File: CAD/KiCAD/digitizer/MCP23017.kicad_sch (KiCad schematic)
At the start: 3 parts, among them P1b Conn_01x06, P3b Conn_01x10, P4a Conn_01x10

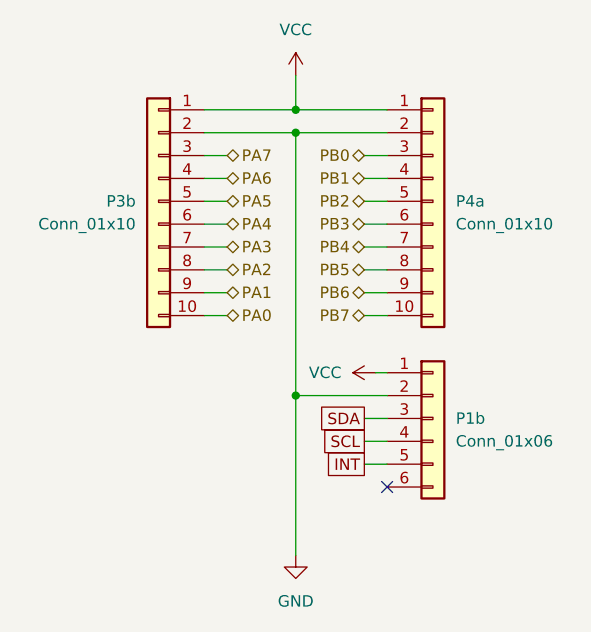
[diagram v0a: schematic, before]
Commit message: one MCP23017 added and routed
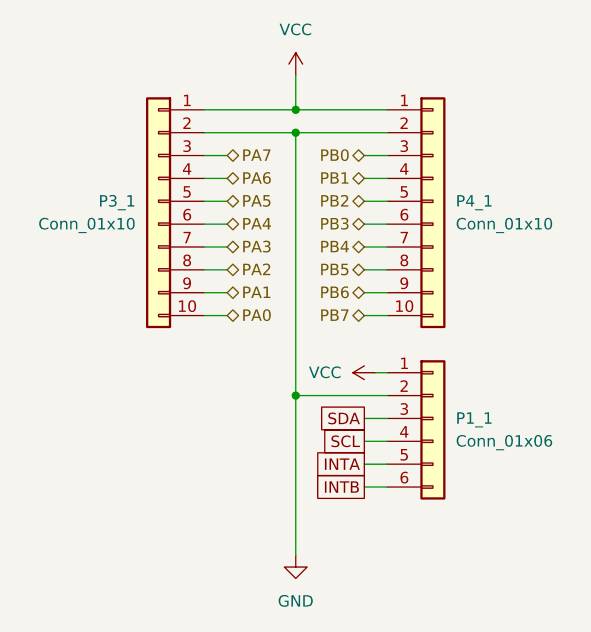
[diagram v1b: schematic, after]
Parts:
- P1_1: renamed from P1b; footprint Connector_PinHeader_2.54mm:PinHeader_1x06_P2.54mm_Vertical -> Connector_PinSocket_2.54mm:PinSocket_1x06_P2.54mm_Vertical
- P3_1: renamed from P3b; footprint Connector_PinHeader_2.54mm:PinHeader_1x10_P2.54mm_Vertical -> Connector_PinSocket_2.54mm:PinSocket_1x10_P2.54mm_Vertical
- P4_1: renamed from P4a; footprint Connector_PinHeader_2.54mm:PinHeader_1x10_P2.54mm_Vertical -> Connector_PinSocket_2.54mm:PinSocket_1x10_P2.54mm_Vertical
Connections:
- net INTB: now reaches P1_1.6 (Pin_6)
- net INT renamed INTA
- no-connect marks 1 -> 0
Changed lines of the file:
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@@
 		(color 0 0 0 0)
 	)
-	(no_connect
-		(at 111.76 102.87)
-	)
 	(wire
 		(pts
@@
 	(wire
 		(pts
+			(xy 109.22 102.87) (xy 111.76 102.87)
+		)
+		(stroke
+			(width 0)
+			(type default)
+		)
+	)
+	(wire
+		(pts
 			(xy 101.6 60.96) (xy 111.76 60.96)
 		)
@@
 		)
 	)
-	(global_label "INT"
+	(global_label "INTA"
 		(shape passive)
 		(at 109.22 100.33 180)
@@
 		)
 		(property "Intersheetrefs" "${INTERSHEET_REFS}"
-			(at 104.4432 100.33 0)
+			(at 103.3546 100.33 0)
 			(effects
 				(font
@@
 		(property "Intersheetrefs" "${INTERSHEET_REFS}"
 			(at 103.778 95.25 0)
+			(effects
+				(font
+					(size 1.27 1.27)
+				)
+				(justify right)
+				(hide yes)
+			)
+		)
+	)
+	(global_label "INTB"
+		(shape passive)
+		(at 109.22 102.87 180)
+		(fields_autoplaced yes)
+		(effects
+			(font
+				(size 1.27 1.27)
+			)
+			(justify right)
+		)
+		(property "Intersheetrefs" "${INTERSHEET_REFS}"
+			(at 103.1732 102.87 0)
 			(effects
 				(font
@@
 					(unit 1)
 				)
-				(path "/7204cdda-0a14-40c0-9dc8-8318dd514140/bcba0207-2ba5-46a1-aca2-aa24991baaf0"
-					(reference "#PWR06")
-					(unit 1)
-				)
 			)
 		)
@@
 		(dnp no)
 		(fields_autoplaced yes)
-		(property "Reference" "#PWR"
+		(property "Reference" "#PWR0101"
 			(at 101.6 60.96 0)
 			(effects
@@
 		(instances
 			(project "digitizer"
-				(path "/7204cdda-0a14-40c0-9dc8-8318dd514140/bcba0207-2ba5-46a1-aca2-aa24991baaf0"
-					(reference "#PWR03")
+				(path "/7204cdda-0a14-40c0-9dc8-8318dd514140/84745f20-6522-4018-95b9-58be475e1f2d"
+					(reference "#PWR0101")
 					(unit 1)
 				)
@@
 		(on_board yes)
 		(dnp no)
-		(property "Reference" "P3b"
+		(property "Reference" "P3_1"
 			(at 83.82 71.1199 0)
 			(effects
@@
 			)
 		)
-		(property "Footprint" "Connector_PinHeader_2.54mm:PinHeader_1x10_P2.54mm_Vertical"
+		(property "Footprint" "Connector_PinSocket_2.54mm:PinSocket_1x10_P2.54mm_Vertical"
 			(at 86.36 71.12 0)
 			(effects
@@
 		(instances
 			(project "digitizer"
-				(path "/7204cdda-0a14-40c0-9dc8-8318dd514140/bcba0207-2ba5-46a1-aca2-aa24991baaf0"
-					(reference "P3b")
+				(path "/7204cdda-0a14-40c0-9dc8-8318dd514140/84745f20-6522-4018-95b9-58be475e1f2d"
+					(reference "P3_1")
 					(unit 1)
 				)
@@
 		(dnp no)
 		(fields_autoplaced yes)
-		(property "Reference" "P4a"
+		(property "Reference" "P4_1"
 			(at 119.38 71.1199 0)
 			(effects
@@
 			)
 		)
-		(property "Footprint" "Connector_PinHeader_2.54mm:PinHeader_1x10_P2.54mm_Vertical"
+		(property "Footprint" "Connector_PinSocket_2.54mm:PinSocket_1x10_P2.54mm_Vertical"
 			(at 116.84 71.12 0)
 			(effects
@@
 			(project "digitizer"
 				(path "/7204cdda-0a14-40c0-9dc8-8318dd514140/84745f20-6522-4018-95b9-58be475e1f2d"
-					(reference "P4a")
-					(unit 1)
-				)
-				(path "/7204cdda-0a14-40c0-9dc8-8318dd514140/bcba0207-2ba5-46a1-aca2-aa24991baaf0"
-					(reference "P4b")
+					(reference "P4_1")
 					(unit 1)
 				)
@@
 					(unit 1)
 				)
-				(path "/7204cdda-0a14-40c0-9dc8-8318dd514140/bcba0207-2ba5-46a1-aca2-aa24991baaf0"
-					(reference "#PWR05")
-					(unit 1)
-				)
 			)
 		)
@@
 		(dnp no)
 		(fields_autoplaced yes)
-		(property "Reference" "P1b"
+		(property "Reference" "P1_1"
 			(at 119.38 95.2499 0)
 			(effects
@@
 			)
 		)
-		(property "Footprint" "Connector_PinHeader_2.54mm:PinHeader_1x06_P2.54mm_Vertical"
+		(property "Footprint" "Connector_PinSocket_2.54mm:PinSocket_1x06_P2.54mm_Vertical"
 			(at 116.84 95.25 0)
 			(effects
@@
 		(instances
 			(project "digitizer"
-				(path "/7204cdda-0a14-40c0-9dc8-8318dd514140/bcba0207-2ba5-46a1-aca2-aa24991baaf0"
-					(reference "P1b")
+				(path "/7204cdda-0a14-40c0-9dc8-8318dd514140/84745f20-6522-4018-95b9-58be475e1f2d"
+					(reference "P1_1")
 					(unit 1)
 				)

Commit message: routing wip take 1
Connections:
- net GND: no longer P3_1.2 (Pin_2), P4_1.2 (Pin_2)
- net VCC: no longer P3_1.1 (Pin_1), P4_1.1 (Pin_1)
- no-connect marks 0 -> 4
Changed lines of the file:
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@@
 	(generator_version "9.0")
 	(paper "USLetter")
-	(junction
-		(at 101.6 60.96)
-		(diameter 0)
-		(color 0 0 0 0)
-	)
-	(junction
-		(at 101.6 63.5)
-		(diameter 0)
-		(color 0 0 0 0)
-	)
-	(junction
-		(at 101.6 92.71)
-		(diameter 0)
-		(color 0 0 0 0)
+	(no_connect
+		(at 91.44 63.5)
+	)
+	(no_connect
+		(at 111.76 63.5)
+	)
+	(no_connect
+		(at 111.76 60.96)
+	)
+	(no_connect
+		(at 91.44 60.96)
 	)
 	(wire
@@
 	(wire
 		(pts
-			(xy 101.6 63.5) (xy 111.76 63.5)
-		)
-		(stroke
-			(width 0)
-			(type default)
-		)
-	)
-	(wire
-		(pts
 			(xy 91.44 76.2) (xy 93.98 76.2)
 		)
@@
 	(wire
 		(pts
-			(xy 101.6 57.15) (xy 101.6 60.96)
-		)
-		(stroke
-			(width 0)
-			(type default)
-		)
-	)
-	(wire
-		(pts
 			(xy 109.22 73.66) (xy 111.76 73.66)
 		)
@@
 	(wire
 		(pts
-			(xy 101.6 60.96) (xy 111.76 60.96)
-		)
-		(stroke
-			(width 0)
-			(type default)
-		)
-	)
-	(wire
-		(pts
-			(xy 91.44 60.96) (xy 101.6 60.96)
-		)
-		(stroke
-			(width 0)
-			(type default)
-		)
-	)
-	(wire
-		(pts
 			(xy 109.22 76.2) (xy 111.76 76.2)
 		)
@@
 		(pts
 			(xy 91.44 81.28) (xy 93.98 81.28)
-		)
-		(stroke
-			(width 0)
-			(type default)
-		)
-	)
-	(wire
-		(pts
-			(xy 101.6 63.5) (xy 101.6 92.71)
-		)
-		(stroke
-			(width 0)
-			(type default)
-		)
-	)
-	(wire
-		(pts
-			(xy 91.44 63.5) (xy 101.6 63.5)
 		)
 		(stroke
@@
 					(unit 1)
 				)
-			)
-		)
-	)
-	(symbol
-		(lib_id "power:VCC")
-		(at 101.6 57.15 0)
-		(unit 1)
-		(exclude_from_sim no)
-		(in_bom yes)
-		(on_board yes)
-		(dnp no)
-		(fields_autoplaced yes)
-		(property "Reference" "#PWR0101"
-			(at 101.6 60.96 0)
-			(effects
-				(font
-					(size 1.27 1.27)
-				)
-				(hide yes)
-			)
-		)
-		(property "Value" "VCC"
-			(at 101.6 52.07 0)
-			(effects
-				(font
-					(size 1.27 1.27)
-				)
-			)
-		)
-		(property "Footprint" ""
-			(at 101.6 57.15 0)
-			(effects
-				(font
-					(size 1.27 1.27)
-				)
-				(hide yes)
-			)
-		)
-		(property "Datasheet" ""
-			(at 101.6 57.15 0)
-			(effects
-				(font
-					(size 1.27 1.27)
-				)
-				(hide yes)
-			)
-		)
-		(property "Description" "Power symbol creates a global label with name \"VCC\""
-			(at 101.6 57.15 0)
-			(effects
-				(font
-					(size 1.27 1.27)
-				)
-				(hide yes)
-			)
-		)
-		(pin "1"
-		)
-		(instances
-			(project "digitizer"
-				(path "/7204cdda-0a14-40c0-9dc8-8318dd514140/84745f20-6522-4018-95b9-58be475e1f2d"
-					(reference "#PWR0101")
-					(unit 1)
-				)

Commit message: remove gerber files
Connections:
- net GND: now also P3_1.2 (Pin_2), P4_1.2 (Pin_2)
- net VCC: now also P3_1.1 (Pin_1), P4_1.1 (Pin_1)
- no-connect marks 4 -> 0
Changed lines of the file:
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@@
 	(generator_version "9.0")
 	(paper "USLetter")
-	(no_connect
-		(at 91.44 63.5)
-	)
-	(no_connect
-		(at 111.76 63.5)
-	)
-	(no_connect
-		(at 111.76 60.96)
-	)
-	(no_connect
-		(at 91.44 60.96)
+	(junction
+		(at 96.52 60.96)
+		(diameter 0)
+		(color 0 0 0 0)
+	)
+	(junction
+		(at 101.6 92.71)
+		(diameter 0)
+		(color 0 0 0 0)
+	)
+	(junction
+		(at 101.6 63.5)
+		(diameter 0)
+		(color 0 0 0 0)
 	)
 	(wire
@@
 	(wire
 		(pts
+			(xy 101.6 63.5) (xy 111.76 63.5)
+		)
+		(stroke
+			(width 0)
+			(type default)
+		)
+	)
+	(wire
+		(pts
+			(xy 96.52 60.96) (xy 111.76 60.96)
+		)
+		(stroke
+			(width 0)
+			(type default)
+		)
+	)
+	(wire
+		(pts
 			(xy 91.44 76.2) (xy 93.98 76.2)
 		)
@@
 	(wire
 		(pts
+			(xy 101.6 63.5) (xy 101.6 92.71)
+		)
+		(stroke
+			(width 0)
+			(type default)
+		)
+	)
+	(wire
+		(pts
 			(xy 91.44 68.58) (xy 93.98 68.58)
 		)
@@
 	(wire
 		(pts
+			(xy 96.52 57.15) (xy 96.52 60.96)
+		)
+		(stroke
+			(width 0)
+			(type default)
+		)
+	)
+	(wire
+		(pts
 			(xy 91.44 81.28) (xy 93.98 81.28)
 		)
@@
 	(wire
 		(pts
+			(xy 91.44 63.5) (xy 101.6 63.5)
+		)
+		(stroke
+			(width 0)
+			(type default)
+		)
+	)
+	(wire
+		(pts
 			(xy 109.22 71.12) (xy 111.76 71.12)
 		)
@@
 		(pts
 			(xy 101.6 92.71) (xy 111.76 92.71)
+		)
+		(stroke
+			(width 0)
+			(type default)
+		)
+	)
+	(wire
+		(pts
+			(xy 96.52 60.96) (xy 91.44 60.96)
 		)
 		(stroke
@@
 					(unit 1)
 				)
+			)
+		)
+	)
+	(symbol
+		(lib_id "power:VCC")
+		(at 96.52 57.15 0)
+		(unit 1)
+		(exclude_from_sim no)
+		(in_bom yes)
+		(on_board yes)
+		(dnp no)
+		(fields_autoplaced yes)
+		(property "Reference" "#PWR010"
+			(at 96.52 60.96 0)
+			(effects
+				(font
+					(size 1.27 1.27)
+				)
+				(hide yes)
+			)
+		)
+		(property "Value" "VCC"
+			(at 96.52 52.07 0)
+			(effects
+				(font
+					(size 1.27 1.27)
+				)
+			)
+		)
+		(property "Footprint" ""
+			(at 96.52 57.15 0)
+			(effects
+				(font
+					(size 1.27 1.27)
+				)
+				(hide yes)
+			)
+		)
+		(property "Datasheet" ""
+			(at 96.52 57.15 0)
+			(effects
+				(font
+					(size 1.27 1.27)
+				)
+				(hide yes)
+			)
+		)
+		(property "Description" "Power symbol creates a global label with name \"VCC\""
+			(at 96.52 57.15 0)
+			(effects
+				(font
+					(size 1.27 1.27)
+				)
+				(hide yes)
+			)
+		)
+		(pin "1"
+		)
+		(instances
+			(project "digitizer"
+				(path "/7204cdda-0a14-40c0-9dc8-8318dd514140/501beeb2-c576-487a-befd-4defb516d792"
+					(reference "#PWR012")
+					(unit 1)
+				)
+				(path "/7204cdda-0a14-40c0-9dc8-8318dd514140/574a7499-7109-4c24-b603-ed58dee53310"
+					(reference "#PWR014")
+					(unit 1)
+				)
+				(path "/7204cdda-0a14-40c0-9dc8-8318dd514140/84745f20-6522-4018-95b9-58be475e1f2d"
+					(reference "#PWR010")
+					(unit 1)
+				)
+				(path "/7204cdda-0a14-40c0-9dc8-8318dd514140/d8fe508a-b704-4fbd-a54e-b6047206bc62"
+					(reference "#PWR011")
+					(unit 1)
+				)
